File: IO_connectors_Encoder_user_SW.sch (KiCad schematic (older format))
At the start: 35 parts, among them IC1 TPD4E001DRLR, IC2 74AUP1G74DC.125, IC3 CD74HC4050PWR, SW1 TL1100CF160Q, SW2 PEC16-2215F-S0024, X1 DS1024-2*20R0, X2 DS1013-16SSIB1, X3 691322110005

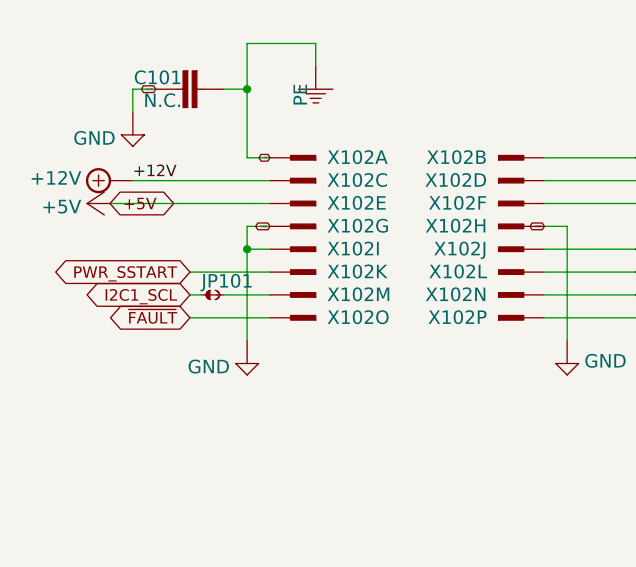
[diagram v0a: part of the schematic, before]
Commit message: Routing FPGA to LCD
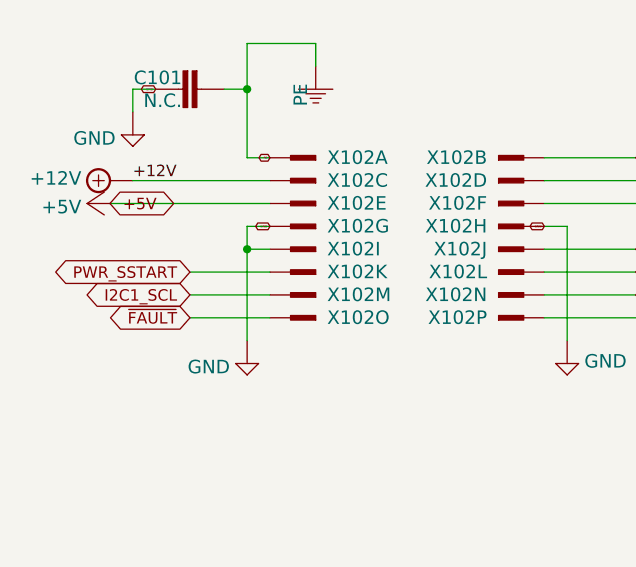
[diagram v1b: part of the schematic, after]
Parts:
- removed JP1: JP2-NOCUT, EEZ DIB MCU r3B4:JP2-NOCUT, symbol IO_connectors_Encoder_user_SW-rescue:JP2-NOCUT-EEZ_DIB_MCU_r3B4-eagle-import
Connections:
- net I2C1_SCL: now also X2.13 (1)
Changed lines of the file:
@@
 Connection ~ 3500 6400
-Wire Wire Line
-	1900 2200 2100 2200
 Wire Wire Line
 	3700 3900 2400 3900
@@
 F 3 "" H 1500 1500 50  0001 C CNN
 	1    1500 1500
-	1    0    0    -1
-$EndComp
-$Comp
-L IO_connectors_Encoder_user_SW-rescue:JP2-NOCUT-EEZ_DIB_MCU_r3B4-eagle-import JP1
-U 1 1 2F430EF2
-P 1800 2200
-AR Path="/848DA6002F430EF2" Ref="JP1"  Part="1"
-AR Path="/5F88C8A0/848DA6002F430EF2" Ref="JP1"  Part="1"
-AR Path="/5F8FDB74/2F430EF2" Ref="JP101"  Part="1"
-F 0 "JP101" H 1800 2225 59  0000 L BNN
-F 1 "JP2-NOCUT" H 1800 2200 50  0001 C CNN
-F 2 "EEZ DIB MCU r3B4:JP2-NOCUT" H 1800 2200 50  0001 C CNN
-F 3 "" H 1800 2200 50  0001 C CNN
-	1    1800 2200
 	1    0    0    -1
 $EndComp
@@
 	1750 2100 2100 2100
 Wire Wire Line
-	1750 2200 1800 2200
-Wire Wire Line
 	1750 2300 2100 2300
 Wire Wire Line
@@
 Wire Wire Line
 	3300 2200 3700 2200
+Wire Wire Line
+	1750 2200 2100 2200
 $EndSCHEMATC
